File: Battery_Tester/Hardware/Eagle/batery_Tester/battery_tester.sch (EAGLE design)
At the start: 8 parts

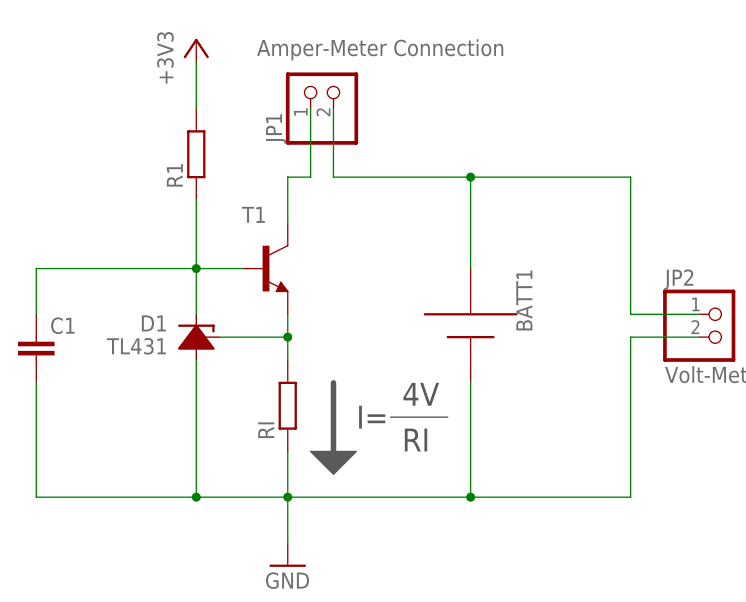
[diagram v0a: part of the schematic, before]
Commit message: Schematic values updated
For Issue #10
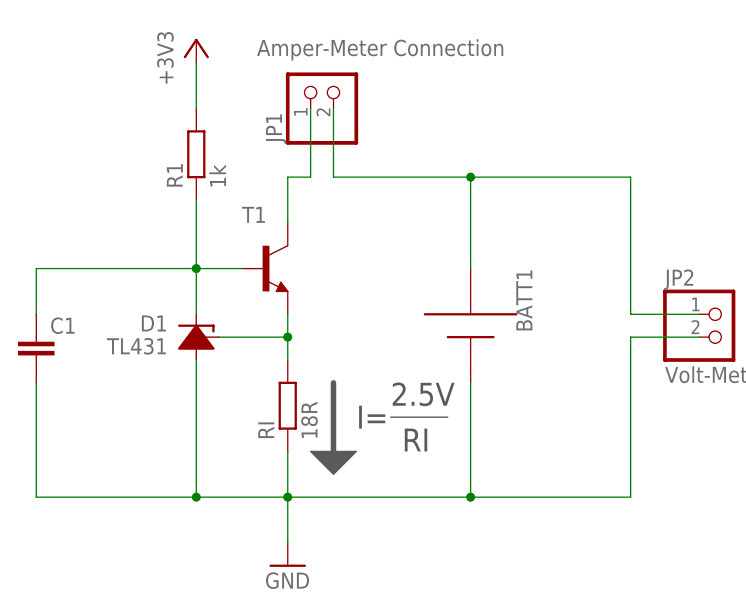
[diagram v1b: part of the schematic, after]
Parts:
- R1: value (none) -> 1k
- RI: value (none) -> 18R
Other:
- note added: "2.5V"
- note removed: "4V"
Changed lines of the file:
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@@
 <part name="D1" library="upra_lib4eagle" deviceset="TL431" device="-TO-92" value="TL431"/>
 <part name="C1" library="resistor" deviceset="C-EU" device="C1206"/>
-<part name="RI" library="resistor" deviceset="R-EU_" device="R1206"/>
+<part name="RI" library="resistor" deviceset="R-EU_" device="R1206" value="18R"/>
 <part name="BATT1" library="upra_lib4eagle" deviceset="BATTERY" device="-PLACEHOLDER"/>
 <part name="+3V1" library="supply1" deviceset="+3V3" device=""/>
@@
 <part name="JP1" library="pinhead" deviceset="PINHD-1X2" device="" value="Amper-Meter Connection"/>
 <part name="JP2" library="pinhead" deviceset="PINHD-1X2" device="" value="Volt-Meter Connection"/>
-<part name="R1" library="resistor" deviceset="R-EU_" device="R1206"/>
+<part name="R1" library="resistor" deviceset="R-EU_" device="R1206" value="1k"/>
 <part name="FRAME1" library="frames" deviceset="A5L-LOC" device="" value="Battery Tester Breadboard"/>
 </parts>
@@
 </polygon>
 <text x="92.71" y="60.96" size="2.54" layer="97">I=</text>
-<text x="97.79" y="63.5" size="2.54" layer="97">4V</text>
+<text x="96.52" y="63.5" size="2.54" layer="97">2.5V</text>
 <text x="97.79" y="58.42" size="2.54" layer="97">RI</text>
 <wire x1="96.52" y1="62.23" x2="102.87" y2="62.23" width="0.1524" layer="97"/>

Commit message: Add files via upload
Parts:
- removed BATT1: BATTERY-PLACEHOLDER, upra_lib4eagle:BATTERY-PLACEHOLDER
- removed JP1: Amper-Meter Connection, pinhead:PINHD-1X2
- removed JP2: Volt-Meter Connection, pinhead:PINHD-1X2
- added BATTERYPACK+, BATTERYPACK-: (no value), wirepad:2,54/1,1
- added DONELED, ERRORLED, PROGRESSLED: (no value), led:LED
- added IC1: (no value), arduino:ARDUINO2009_22
- added R2, R3: 1 kΩ, resistor:R-EU_WSC2515
- added R4, R5, R6: 220 kΩ, resistor:R-EU_WSC2515
- added U$1: MICRO-SD_BREAKOUT-FLAT, upra_lib4eagle:MICRO-SD_BREAKOUT-FLAT
- C1: value (none) -> 100 µF; device resistor:C-EUC1206 -> resistor:C-EUC4532
- D1: value TL431 -> TL431-TO-92
- R1: value 1k -> 1 kΩ; device resistor:R-EU_R1206 -> resistor:R-EU_WSC2515
- RI: value 18R -> 18 Ω; device resistor:R-EU_R1206 -> resistor:R-EU_WSC2515
- T1: device transistor-neu-to92:BC368-NPN-TO92-ECB -> transistor:-NPN-TO92
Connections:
- removed net +3V3: R1.2
- removed net N$1 (its old number): JP1.1, T1.C
- new net +5V: IC1G$2.+5V, R1.2
- new net 3V3: IC1G$3.+3V3, U$1.3V3
- new net ANALOGIN: IC1G$1.A0, R2.1, R3.2
- new net BATTERYPACK+: BATTERYPACK+.P, R2.2, T1.C
- new net CLK: IC1G$1.13, U$1.SCK
- new net CS: IC1G$1.2, U$1.CS
- new net DONELED: IC1G$1.5, R5.2
- new net ERRORLED: IC1G$1.3, R4.2
- new net MISO: IC1G$1.12, U$1.MISO
- new net MOSI: IC1G$1.11, U$1.MOSI
- new net N$4: PROGRESSLED.A, R6.1
- new net N$5: DONELED.A, R5.1
- new net PROGRESSLED: IC1G$1.4, R6.2
- net GND: now also BATTERYPACK-.P, DONELED.C, ERRORLED.C, PROGRESSLED.C, R3.1, U$1.GND; no longer BATT1.+, JP2.2
- net N$2: now also ERRORLED.A, R4.1; no longer BATT1.-, JP1.2, JP2.1
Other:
- note removed: "2.5V"
- note removed: "I="
- note removed: "RI"
